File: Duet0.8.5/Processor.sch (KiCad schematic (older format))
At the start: 43 parts, among them J21 JTAG, J26 GND, U1 ATSAM3X8E, X2 CRYSTAL_4PIN

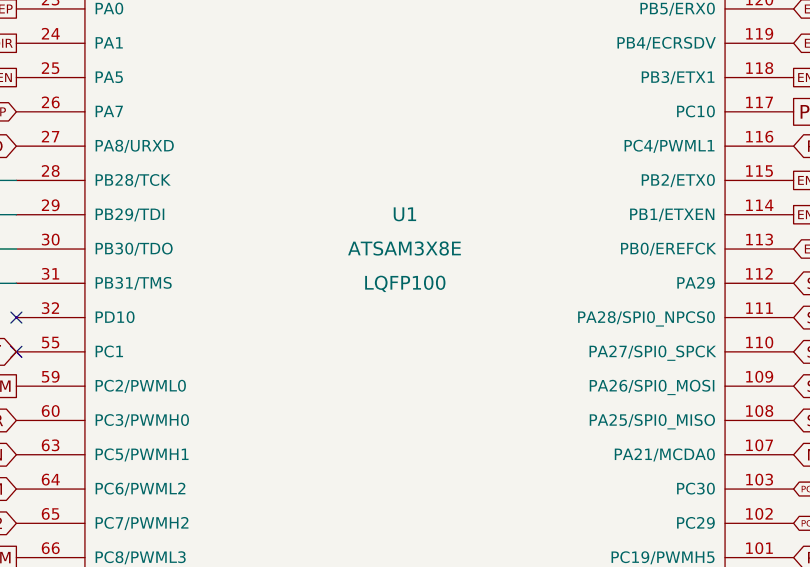
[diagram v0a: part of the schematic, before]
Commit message: Schematic footprint error correction
The schematic specified the SAM3X8E footprint as a LQFP100. this
corrects this to LQFP144
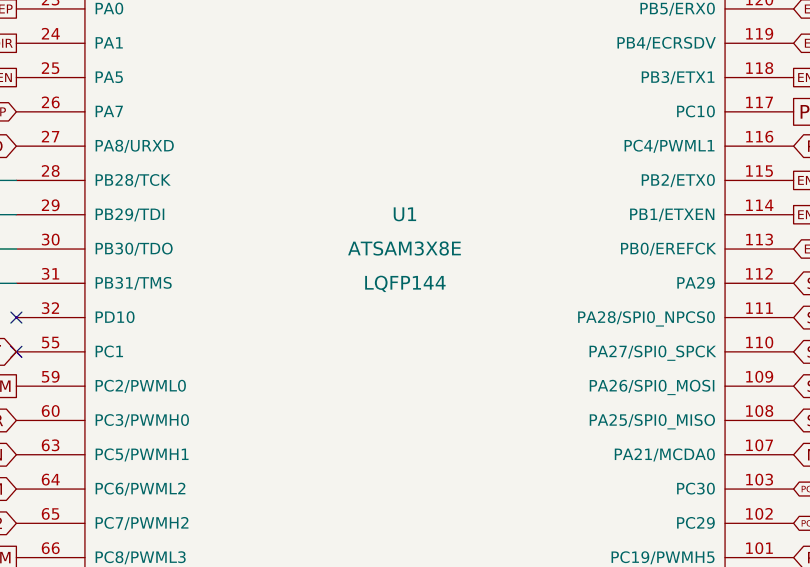
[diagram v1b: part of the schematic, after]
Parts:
- U1: footprint LQFP100 -> LQFP144
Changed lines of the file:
@@
 EESchema Schematic File Version 2
+LIBS:Duet0.85-rescue
 LIBS:power
-LIBS:device
 LIBS:transistors
 LIBS:conn
@@
 LIBS:memory
 LIBS:xilinx
-LIBS:special
 LIBS:microcontrollers
 LIBS:dsp
@@
 LIBS:FE
 LIBS:Duet0.85-cache
-EELAYER 27 0
+EELAYER 25 0
 EELAYER END
 $Descr A2 23386 16535
@@
 U 1 1 53B059FA
 P 13600 12800
+AR Path="/53B059FA" Ref="C90"  Part="1"
+AR Path="/50523307/53B059FA" Ref="C90"  Part="1"
 F 0 "C90" H 13625 12850 30  0000 L CNN
 F 1 "10nF" H 13625 12750 30  0000 L CNN
@@
 F 0 "U1" H 11500 10850 60  0000 C CNN
 F 1 "ATSAM3X8E" H 11500 10700 60  0000 C CNN
-F 2 "LQFP100" H 11500 10550 60  0000 C CNN
+F 2 "LQFP144" H 11500 10550 60  0000 C CNN
 F 3 "" H 11500 10200 60  0001 C CNN
 	1    11500 10200
